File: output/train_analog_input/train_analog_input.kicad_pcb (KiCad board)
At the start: 2 copper layers, 65 x 40 mm, 29 parts, among them J1 Screw_Terminal_2P, J2 Screw_Terminal_2P, J3 Screw_Terminal_2P, J4 Screw_Terminal_2P, J5 PinHeader_1x04, U1 ADS1115

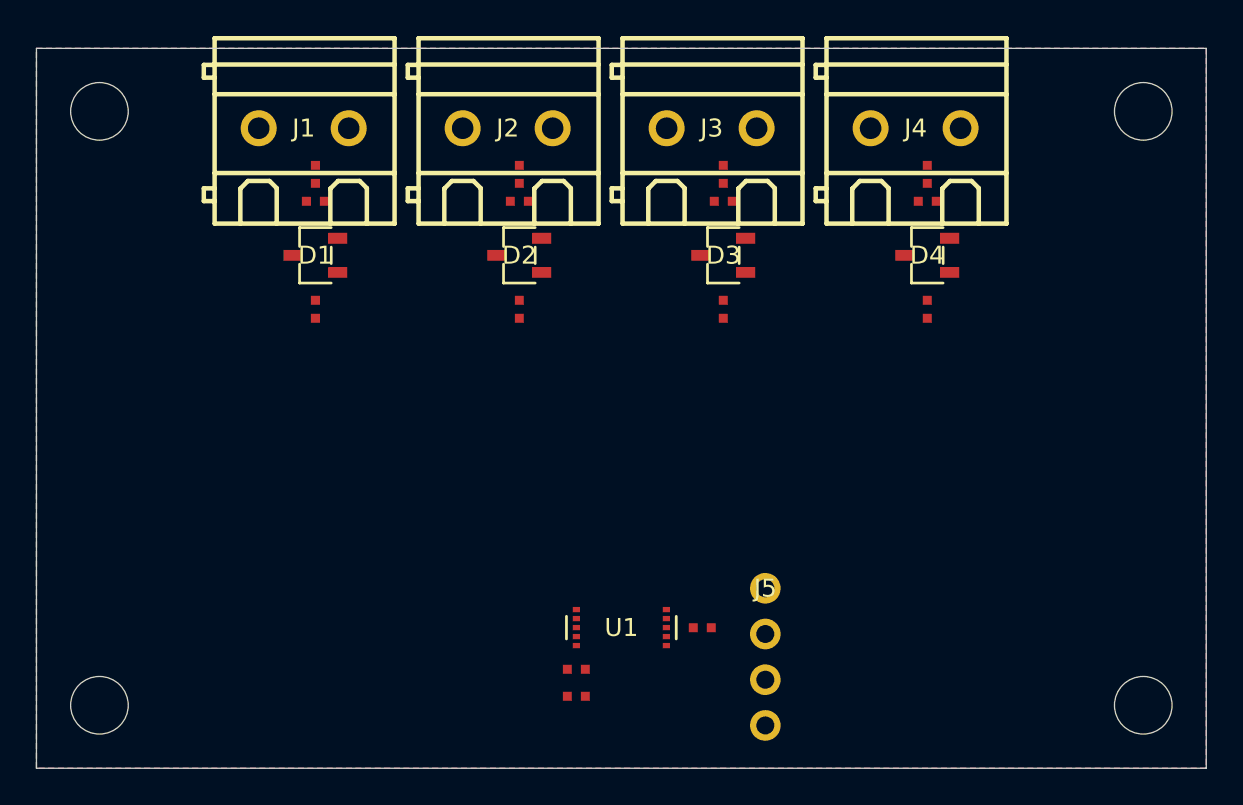
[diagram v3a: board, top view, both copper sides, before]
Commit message: chore(output): update board renders, evidence images, and clean up artifacts
- Updated renders for all 5 training boards (analog, ethernet, mcu, power, relay)
- Added component evidence renders (122 component isolation boards)
- Removed stale train_relay crops, backups, and broken files
- Added easyeda2kicad footprint libraries for train boards

Co-Authored-By: Claude Opus 4.6 (1M context) <noreply@anthropic.com>
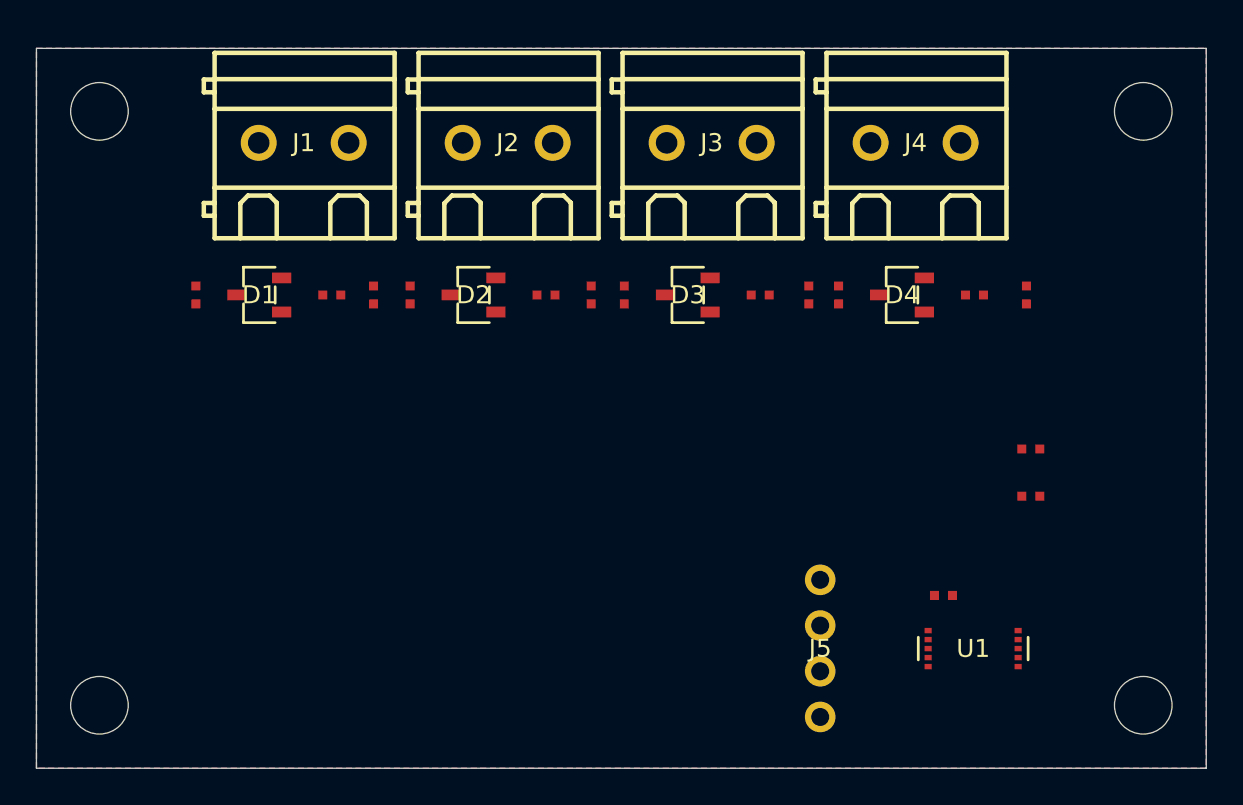
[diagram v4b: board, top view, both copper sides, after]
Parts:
- moved R10 28.7 mm to (55.2, 22.3)
- moved R9 27.0 mm to (55.2, 24.9)
- moved U1 19.6 mm to (52.0, 33.4), turned to 180 degrees
- moved C1 13.5 mm to (50.4, 30.4)
- moved R7 8.67 mm to (55.0, 13.7)
- moved C2 8.43 mm to (8.86, 13.7), turned to 90 degrees
- moved R5 8.21 mm to (42.9, 13.7)
- moved C3 7.99 mm to (20.8, 13.7), turned to 90 degrees
- moved R3 7.80 mm to (30.8, 13.7)
- moved C4 7.57 mm to (32.7, 13.7), turned to 90 degrees
- moved R1 7.44 mm to (18.7, 13.7)
- moved C5 7.17 mm to (44.6, 13.7), turned to 90 degrees
- moved J5 4.52 mm to (43.5, 33.3)
- moved D1 3.81 mm to (12.4, 13.7)
- moved D2 3.36 mm to (24.3, 13.7)
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
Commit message: chore(wip): snapshot broken tree before placement redesign
KNOWN BROKEN — committed as-is to preserve state before redesign:
- bottom-up rewrite stages untracked since Apr 4 (subcircuit_layout.py,
  board_packer.py, verified_iteration.py + tests) fail on missing
  geometry.convex_hull import
- circular import in orchestrator/models crashes the eval suite
- regenerated training board outputs + component evidence renders

Eval gate bypassed deliberately (suite cannot even import).

Co-Authored-By: Claude Fable 5 <noreply@anthropic.com>
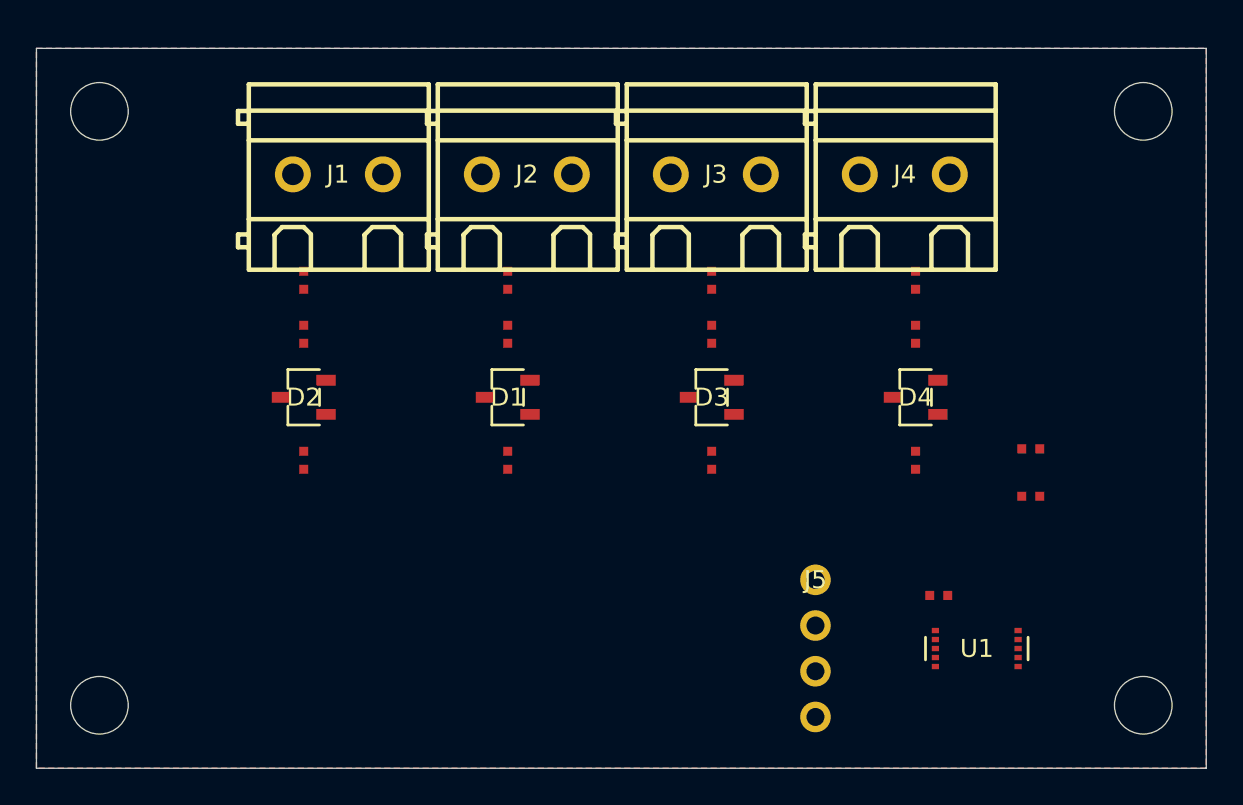
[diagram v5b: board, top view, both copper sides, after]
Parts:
- moved C2 19.6 mm to (26.2, 22.9)
- moved R3 16.0 mm to (14.8, 12.9)
- moved D1 14.9 mm to (26.2, 19.4)
- moved R4 13.6 mm to (14.8, 15.9), turned to 90 degrees
- moved D2 11.0 mm to (14.8, 19.4)
- moved C3 10.9 mm to (14.8, 22.9)
- moved C4 10.4 mm to (37.5, 22.9)
- moved C5 10.1 mm to (48.9, 22.9)
- moved R2 10.0 mm to (26.2, 15.9), turned to 90 degrees
- moved R1 7.50 mm to (26.2, 12.9)
- moved R7 6.21 mm to (48.9, 12.9)
- moved D3 5.84 mm to (37.5, 19.4)
- moved D4 5.74 mm to (48.9, 19.4)
- moved R5 5.46 mm to (37.5, 12.9)
- moved R8 3.93 mm to (48.9, 15.9), turned to 90 degrees
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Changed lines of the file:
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@@
   (title_block
     (title "AnalogInputTraining")
-    (date "2026-03-30")
+    (date "2026-04-02")
     (rev "v1")
   )
@@
   (footprint "MSOP-10"
     (layer "F.Cu")
-    (at 52.05 33.35 180.0)
+    (at 52.25 33.35 180.0)
     (attr smd)
     (property "Reference" "U1"
@@
     )
     (fp_line
-      (start -2.95 -1.65)
-      (end 2.95 -1.65)
+      (start -2.75 -1.65)
+      (end 2.75 -1.65)
       (layer "F.CrtYd")
       (width 0.153)
     )
     (fp_line
-      (start 2.95 -1.65)
-      (end 2.95 1.65)
+      (start 2.75 -1.65)
+      (end 2.75 1.65)
       (layer "F.CrtYd")
       (width 0.153)
     )
     (fp_line
-      (start 2.95 1.65)
-      (end -2.95 1.65)
+      (start 2.75 1.65)
+      (end -2.75 1.65)
       (layer "F.CrtYd")
       (width 0.153)
     )
     (fp_line
-      (start -2.95 1.65)
-      (end -2.95 -1.65)
+      (start -2.75 1.65)
+      (end -2.75 -1.65)
       (layer "F.CrtYd")
       (width 0.153)
     )
     (fp_line
-      (start -3.05 -0.63)
-      (end -3.05 0.63)
+      (start -2.85 -0.63)
+      (end -2.85 0.63)
       (layer "F.SilkS")
       (width 0.153)
     )
     (fp_line
-      (start 3.05 -0.63)
-      (end 3.05 0.63)
+      (start 2.85 -0.63)
+      (end 2.85 0.63)
       (layer "F.SilkS")
       (width 0.153)
     )
     (pad "1" smd rect
-      (at -2.5 -1.0)
+      (at -2.3 -1.0)
       (size 0.4 0.3)
       (layers "F.Cu" "F.Paste" "F.Mask")
@@
     )
     (pad "2" smd rect
-      (at -2.5 -0.5)
+      (at -2.3 -0.5)
       (size 0.4 0.3)
       (layers "F.Cu" "F.Paste" "F.Mask")
     )
     (pad "3" smd rect
-      (at -2.5 0.0)
+      (at -2.3 0.0)
       (size 0.4 0.3)
       (layers "F.Cu" "F.Paste" "F.Mask")
@@
     )
     (pad "4" smd rect
-      (at -2.5 0.5)
+      (at -2.3 0.5)
       (size 0.4 0.3)
       (layers "F.Cu" "F.Paste" "F.Mask")
@@
     )
     (pad "5" smd rect
-      (at -2.5 1.0)
+      (at -2.3 1.0)
       (size 0.4 0.3)
       (layers "F.Cu" "F.Paste" "F.Mask")
@@
     )
     (pad "6" smd rect
-      (at 2.5 1.0)
+      (at 2.3 1.0)
       (size 0.4 0.3)
       (layers "F.Cu" "F.Paste" "F.Mask")
@@
     )
     (pad "7" smd rect
-      (at 2.5 0.5)
+      (at 2.3 0.5)
       (size 0.4 0.3)
       (layers "F.Cu" "F.Paste" "F.Mask")
@@
     )
     (pad "8" smd rect
-      (at 2.5 0.0)
+      (at 2.3 0.0)
       (size 0.4 0.3)
       (layers "F.Cu" "F.Paste" "F.Mask")
@@
     )
     (pad "9" smd rect
-      (at 2.5 -0.5)
+      (at 2.3 -0.5)
       (size 0.4 0.3)
       (layers "F.Cu" "F.Paste" "F.Mask")
@@
     )
     (pad "10" smd rect
-      (at 2.5 -1.0)
+      (at 2.3 -1.0)
       (size 0.4 0.3)
       (layers "F.Cu" "F.Paste" "F.Mask")
@@
   (footprint "Capacitor_SMD:C_0402_1005Metric"
     (layer "F.Cu")
-    (at 50.3993 30.395 180.0)
+    (at 50.1353 30.395 180.0)
     (attr smd)
     (property "Reference" "C1"
@@
   (footprint "Resistor_SMD:R_0402_1005Metric"
     (layer "F.Cu")
-    (at 18.73 13.7 90.0)
+    (at 26.1833 12.8875 90.0)
     (attr smd)
     (property "Reference" "R1"
@@
   (footprint "Resistor_SMD:R_0402_1005Metric"
     (layer "F.Cu")
-    (at 16.41 13.7 180.0)
+    (at 26.1833 15.8875 90.0)
     (attr smd)
     (property "Reference" "R2"
@@
   (footprint "easyeda2kicad:SOT-23-3_L2.9-W1.6-P1.90-LS2.8-BR"
     (layer "F.Cu")
-    (at 12.385 13.7 0.0)
+    (at 26.1833 19.3875 0.0)
     (attr smd)
     (property "Reference" "D1"
@@
   (footprint "Capacitor_SMD:C_0402_1005Metric"
     (layer "F.Cu")
-    (at 8.86 13.7 90.0)
+    (at 26.1833 22.8875 90.0)
     (attr smd)
     (property "Reference" "C2"
@@
   (footprint "easyeda2kicad:CONN-TH_2P-P5.00_WJ128V-5.0-2P"
     (layer "F.Cu")
-    (at 14.85 5.25 0.0)
+    (at 16.75 7.0 0.0)
     (attr through_hole)
     (property "Reference" "J1"
@@
     (model "${KICAD10_3DMODEL_DIR}/TerminalBlock_Phoenix.3dshapes/TerminalBlock_Phoenix_MKDS-1,5-2-5.08_1x02_P5.08mm_Horizontal.step"
       (offset
-        (xyz 0.0 0.0 0.0)
+        (xyz -2.5 0.0 0.0)
       )
       (scale
@@
   (footprint "Resistor_SMD:R_0402_1005Metric"
     (layer "F.Cu")
-    (at 30.8233 13.7 90.0)
+    (at 14.85 12.8875 90.0)
     (attr smd)
     (property "Reference" "R3"
@@
   (footprint "Resistor_SMD:R_0402_1005Metric"
     (layer "F.Cu")
-    (at 28.3133 13.7 180.0)
+    (at 14.85 15.8875 90.0)
     (attr smd)
     (property "Reference" "R4"
@@
   (footprint "easyeda2kicad:SOT-23-3_L2.9-W1.6-P1.90-LS2.8-BR"
     (layer "F.Cu")
-    (at 24.2883 13.7 0.0)
+    (at 14.85 19.3875 0.0)
     (attr smd)
     (property "Reference" "D2"
@@
   (footprint "Capacitor_SMD:C_0402_1005Metric"
     (layer "F.Cu")
-    (at 20.7633 13.7 90.0)
+    (at 14.85 22.8875 90.0)
     (attr smd)
     (property "Reference" "C3"
@@
   (footprint "easyeda2kicad:CONN-TH_2P-P5.00_WJ128V-5.0-2P"
     (layer "F.Cu")
-    (at 26.1833 5.25 0.0)
+    (at 27.25 7.0 0.0)
     (attr through_hole)
     (property "Reference" "J2"
@@
     (model "${KICAD10_3DMODEL_DIR}/TerminalBlock_Phoenix.3dshapes/TerminalBlock_Phoenix_MKDS-1,5-2-5.08_1x02_P5.08mm_Horizontal.step"
       (offset
-        (xyz 0.0 0.0 0.0)
+        (xyz -2.5 0.0 0.0)
       )
       (scale
@@
   (footprint "Resistor_SMD:R_0402_1005Metric"
     (layer "F.Cu")
-    (at 42.9167 13.7 90.0)
+    (at 37.5167 12.8875 90.0)
     (attr smd)
     (property "Reference" "R5"
@@
   (footprint "Resistor_SMD:R_0402_1005Metric"
     (layer "F.Cu")
-    (at 40.2167 13.7 180.0)
+    (at 37.5167 15.8875 90.0)
     (attr smd)
     (property "Reference" "R6"
@@
   (footprint "easyeda2kicad:SOT-23-3_L2.9-W1.6-P1.90-LS2.8-BR"
     (layer "F.Cu")
-    (at 36.1917 13.7 0.0)
+    (at 37.5167 19.3875 0.0)
     (attr smd)
     (property "Reference" "D3"
@@
   (footprint "Capacitor_SMD:C_0402_1005Metric"
     (layer "F.Cu")
-    (at 32.6667 13.7 90.0)
+    (at 37.5167 22.8875 90.0)
     (attr smd)
     (property "Reference" "C4"
@@
   (footprint "easyeda2kicad:CONN-TH_2P-P5.00_WJ128V-5.0-2P"
     (layer "F.Cu")
-    (at 37.5167 5.25 0.0)
+    (at 37.75 7.0 0.0)
     (attr through_hole)
     (property "Reference" "J3"
@@
     (model "${KICAD10_3DMODEL_DIR}/TerminalBlock_Phoenix.3dshapes/TerminalBlock_Phoenix_MKDS-1,5-2-5.08_1x02_P5.08mm_Horizontal.step"
       (offset
-        (xyz 0.0 0.0 0.0)
+        (xyz -2.5 0.0 0.0)
       )
       (scale
@@
   (footprint "Resistor_SMD:R_0402_1005Metric"
     (layer "F.Cu")
-    (at 55.01 13.7 90.0)
+    (at 48.85 12.8875 90.0)
     (attr smd)
     (property "Reference" "R7"
@@
   (footprint "Resistor_SMD:R_0402_1005Metric"
     (layer "F.Cu")
-    (at 52.12 13.7 180.0)
+    (at 48.85 15.8875 90.0)
     (attr smd)
     (property "Reference" "R8"
@@
   (footprint "easyeda2kicad:SOT-23-3_L2.9-W1.6-P1.90-LS2.8-BR"
     (layer "F.Cu")
-    (at 48.095 13.7 0.0)
+    (at 48.85 19.3875 0.0)
     (attr smd)
     (property "Reference" "D4"
@@
       )
     )
-    (property "Group" "Analog Inputs"
-      (at 0 0 0)
-      (layer "F.Fab")
-      (effects
-        (font
-          (size 1.0 1.0)
-        )
-        (hide yes)
-      )
-    )
     (fp_text user "%R"
       (at 0.0 0.0)
@@
   (footprint "Capacitor_SMD:C_0402_1005Metric"
     (layer "F.Cu")
-    (at 44.57 13.7 90.0)
+    (at 48.85 22.8875 90.0)
     (attr smd)
     (property "Reference" "C5"
@@
   (footprint "easyeda2kicad:CONN-TH_2P-P5.00_WJ128V-5.0-2P"
     (layer "F.Cu")
-    (at 48.85 5.25 0.0)
+    (at 48.25 7.0 0.0)
     (attr through_hole)
     (property "Reference" "J4"
@@
     (model "${KICAD10_3DMODEL_DIR}/TerminalBlock_Phoenix.3dshapes/TerminalBlock_Phoenix_MKDS-1,5-2-5.08_1x02_P5.08mm_Horizontal.step"
       (offset
-        (xyz 0.0 0.0 0.0)
+        (xyz -2.5 0.0 0.0)
       )
       (scale
@@
   (footprint "PinHeader_1x04"
     (layer "F.Cu")
-    (at 43.5493 33.34 0.0)
+    (at 43.2853 29.53 0.0)
     (attr through_hole)
     (property "Reference" "J5"
@@
     )
     (fp_line
-      (start -1.85 -5.66)
-      (end 1.85 -5.66)
+      (start -1.85 -1.85)
+      (end 1.85 -1.85)
       (layer "F.CrtYd")
       (width 0.153)
     )
     (fp_line
-      (start 1.85 -5.66)
-      (end 1.85 5.66)
+      (start 1.85 -1.85)
+      (end 1.85 9.47)
       (layer "F.CrtYd")
       (width 0.153)
     )
     (fp_line
-      (start 1.85 5.66)
-      (end -1.85 5.66)
+      (start 1.85 9.47)
+      (end -1.85 9.47)
       (layer "F.CrtYd")
       (width 0.153)
     )
     (fp_line
-      (start -1.85 5.66)
-      (end -1.85 -5.66)
+      (start -1.85 9.47)
+      (end -1.85 -1.85)
       (layer "F.CrtYd")
       (width 0.153)
     )
     (pad "1" thru_hole circle
-      (at 0.0 -3.81)
+      (at 0.0 0.0)
       (size 1.7 1.7)
       (layers "F.Cu" "B.Cu" "F.Mask" "B.Mask")
@@
     )
     (pad "2" thru_hole circle
-      (at 0.0 -1.27)
+      (at 0.0 2.54)
       (size 1.7 1.7)
       (layers "F.Cu" "B.Cu" "F.Mask" "B.Mask")
@@
     )
     (pad "3" thru_hole circle
-      (at 0.0 1.27)
+      (at 0.0 5.08)
       (size 1.7 1.7)
       (layers "F.Cu" "B.Cu" "F.Mask" "B.Mask")
@@
     )
     (pad "4" thru_hole circle
-      (at 0.0 3.81)
+      (at 0.0 7.62)
       (size 1.7 1.7)
       (layers "F.Cu" "B.Cu" "F.Mask" "B.Mask")
